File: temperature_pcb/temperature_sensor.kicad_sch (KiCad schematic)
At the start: 15 parts, among them J1 Screw_Terminal_01x02, M1 MAX31865-adafruit-module, M10 MAX31865-adafruit-module, M11 MAX31865-adafruit-module, M12 MAX31865-adafruit-module, M13 MAX31865-adafruit-module, M2 MAX31865-adafruit-module, M3 MAX31865-adafruit-module, M4 MAX31865-adafruit-module, M5 MAX31865-adafruit-module, M6 MAX31865-adafruit-module, M7 MAX31865-adafruit-module, M8 MAX31865-adafruit-module, M9 MAX31865-adafruit-module

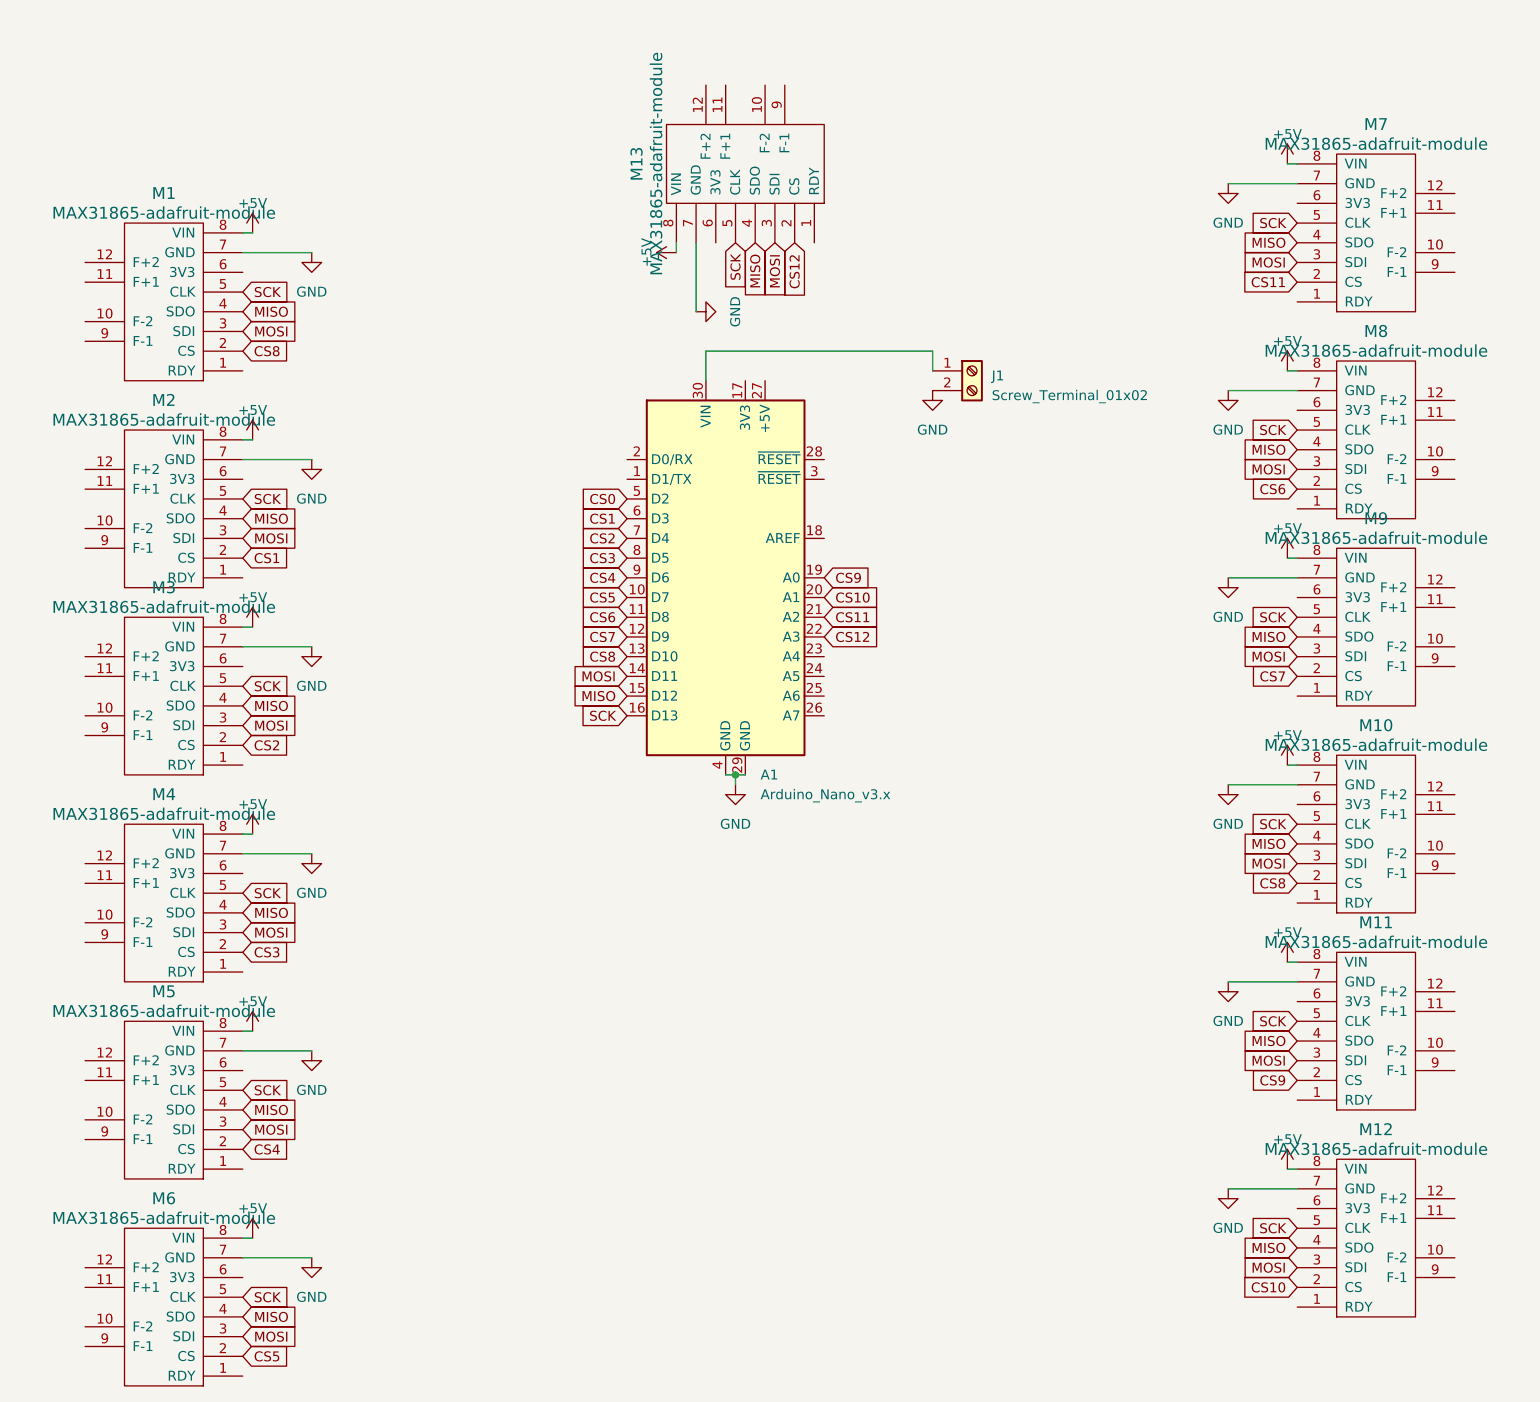
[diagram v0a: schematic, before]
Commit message: first version of the pcb for the temperature sensors
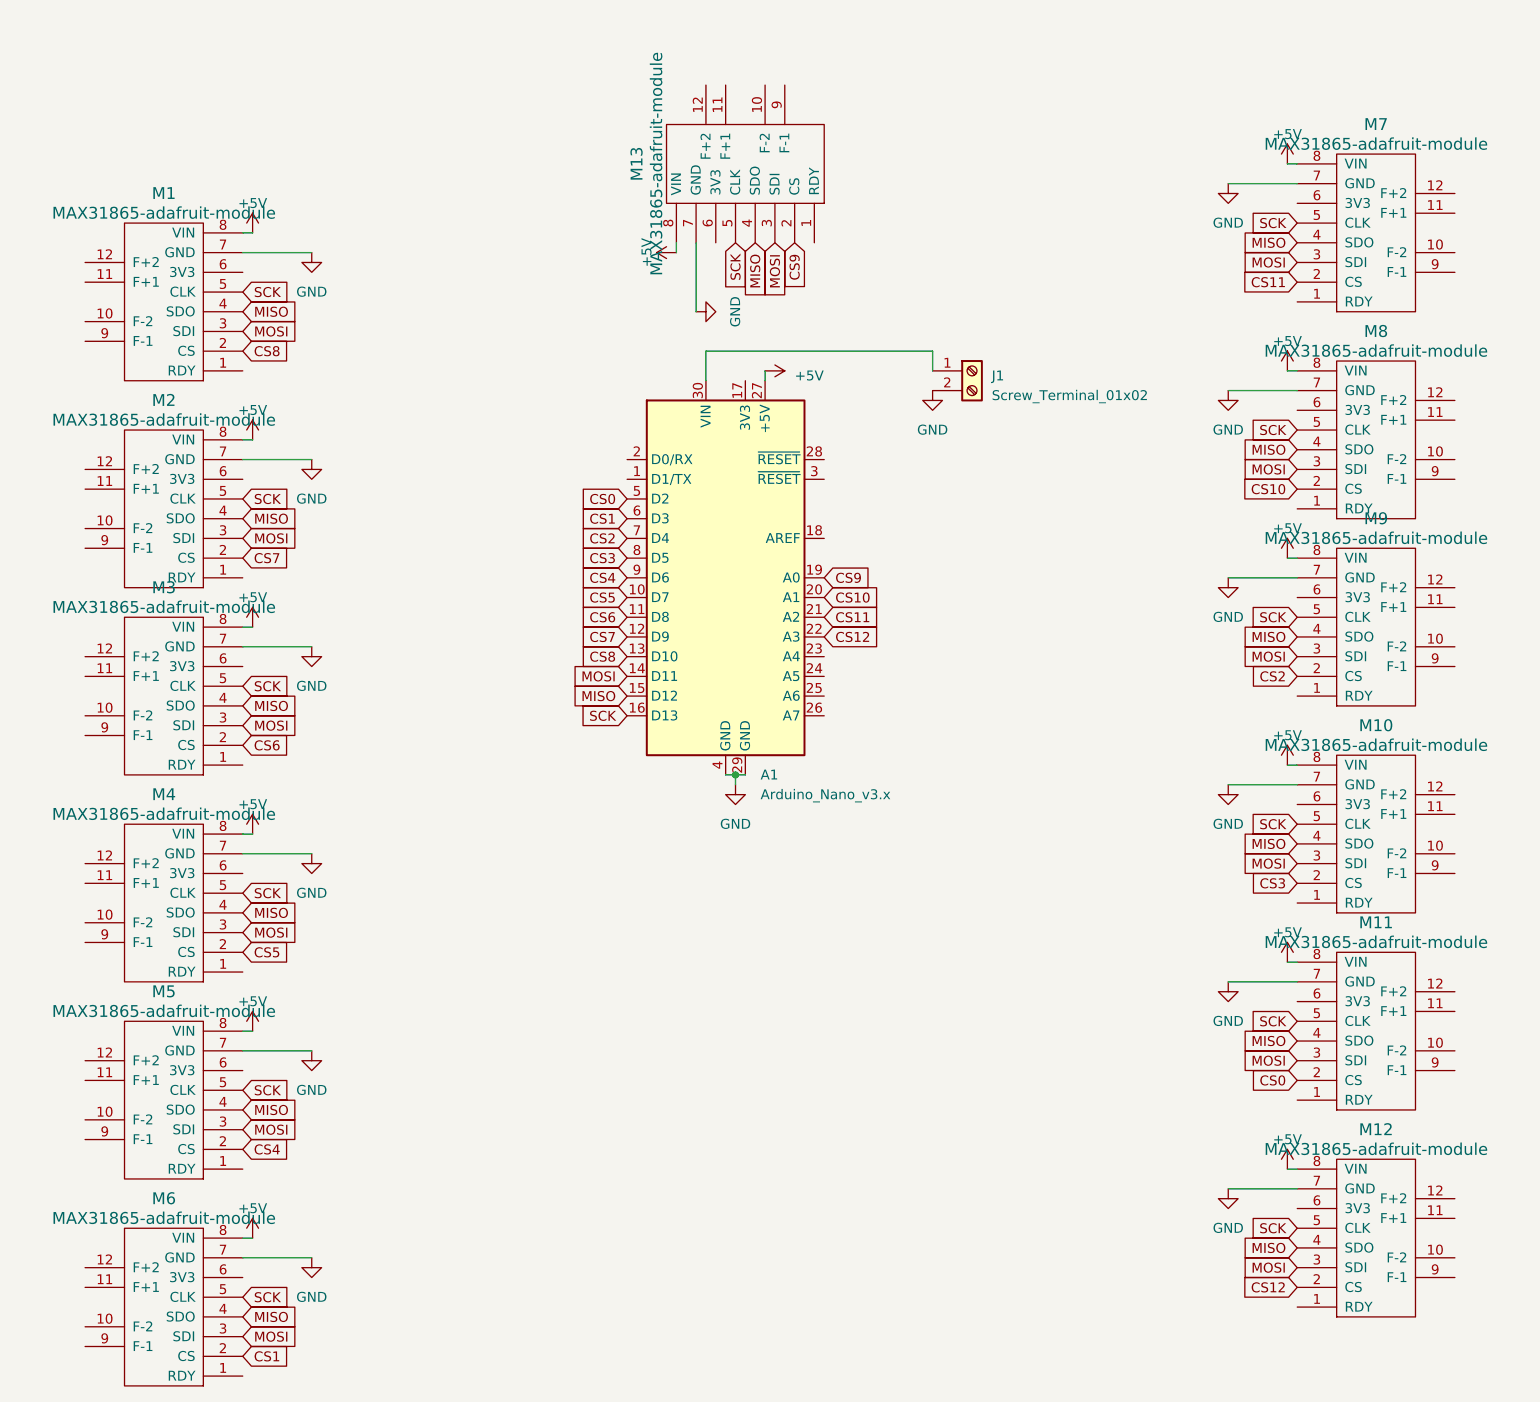
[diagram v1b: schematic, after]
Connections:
- net +5V: now also A1.27 (+5V)
- net CS0: now also M11.2 (CS)
- net CS1: now also M6.2 (CS); no longer M2.2 (CS)
- net CS10: now also M8.2 (CS); no longer M12.2 (CS)
- net CS12: now also M12.2 (CS); no longer M13.2 (CS)
- net CS2: now also M9.2 (CS); no longer M3.2 (CS)
- net CS3: now also M10.2 (CS); no longer M4.2 (CS)
- net CS5: now also M4.2 (CS); no longer M6.2 (CS)
- net CS6: now also M3.2 (CS); no longer M8.2 (CS)
- net CS7: now also M2.2 (CS); no longer M9.2 (CS)
- net CS8: no longer M10.2 (CS)
- net CS9: now also M13.2 (CS); no longer M11.2 (CS)
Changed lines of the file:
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@@
+    (stroke (width 0) (type default))
+  )
+  (wire (pts (xy 140.97 55.88) (xy 140.97 57.15))
     (stroke (width 0) (type default))
   )
@@
     )
   )
-  (global_label "CS2" (shape input) (at 73.66 104.14 0) (fields_autoplaced)
+  (global_label "CS6" (shape input) (at 73.66 104.14 0) (fields_autoplaced)
     (effects (font (size 1.27 1.27)) (justify left))
     (property "Intersheetrefs" "${INTERSHEET_REFS}" (at 80.2548 104.14 0)
@@
     )
   )
-  (global_label "CS12" (shape input) (at 144.78 39.37 270) (fields_autoplaced)
-    (effects (font (size 1.27 1.27)) (justify right))
-    (property "Intersheetrefs" "${INTERSHEET_REFS}" (at 144.78 47.1743 90)
+  (global_label "CS9" (shape input) (at 144.78 39.37 270) (fields_autoplaced)
+    (effects (font (size 1.27 1.27)) (justify right))
+    (property "Intersheetrefs" "${INTERSHEET_REFS}" (at 144.78 45.9648 90)
       (effects (font (size 1.27 1.27)) (justify right) hide)
     )
@@
     )
   )
-  (global_label "CS7" (shape input) (at 209.55 95.25 180) (fields_autoplaced)
+  (global_label "CS2" (shape input) (at 209.55 95.25 180) (fields_autoplaced)
     (effects (font (size 1.27 1.27)) (justify right))
     (property "Intersheetrefs" "${INTERSHEET_REFS}" (at 202.9552 95.25 0)
@@
     )
   )
-  (global_label "CS10" (shape input) (at 209.55 173.99 180) (fields_autoplaced)
+  (global_label "CS12" (shape input) (at 209.55 173.99 180) (fields_autoplaced)
     (effects (font (size 1.27 1.27)) (justify right))
     (property "Intersheetrefs" "${INTERSHEET_REFS}" (at 201.7457 173.99 0)
@@
     )
   )
-  (global_label "CS9" (shape input) (at 209.55 147.32 180) (fields_autoplaced)
+  (global_label "CS0" (shape input) (at 209.55 147.32 180) (fields_autoplaced)
     (effects (font (size 1.27 1.27)) (justify right))
     (property "Intersheetrefs" "${INTERSHEET_REFS}" (at 202.9552 147.32 0)
@@
     )
   )
-  (global_label "CS1" (shape input) (at 73.66 80.01 0) (fields_autoplaced)
+  (global_label "CS7" (shape input) (at 73.66 80.01 0) (fields_autoplaced)
     (effects (font (size 1.27 1.27)) (justify left))
     (property "Intersheetrefs" "${INTERSHEET_REFS}" (at 80.2548 80.01 0)
@@
     )
   )
-  (global_label "CS5" (shape input) (at 73.66 182.88 0) (fields_autoplaced)
+  (global_label "CS1" (shape input) (at 73.66 182.88 0) (fields_autoplaced)
     (effects (font (size 1.27 1.27)) (justify left))
     (property "Intersheetrefs" "${INTERSHEET_REFS}" (at 80.2548 182.88 0)
@@
     )
   )
-  (global_label "CS8" (shape input) (at 209.55 121.92 180) (fields_autoplaced)
+  (global_label "CS3" (shape input) (at 209.55 121.92 180) (fields_autoplaced)
     (effects (font (size 1.27 1.27)) (justify right))
     (property "Intersheetrefs" "${INTERSHEET_REFS}" (at 202.9552 121.92 0)
@@
     )
   )
-  (global_label "CS6" (shape input) (at 209.55 71.12 180) (fields_autoplaced)
-    (effects (font (size 1.27 1.27)) (justify right))
-    (property "Intersheetrefs" "${INTERSHEET_REFS}" (at 202.9552 71.12 0)
+  (global_label "CS10" (shape input) (at 209.55 71.12 180) (fields_autoplaced)
+    (effects (font (size 1.27 1.27)) (justify right))
+    (property "Intersheetrefs" "${INTERSHEET_REFS}" (at 201.7457 71.12 0)
       (effects (font (size 1.27 1.27)) (justify right) hide)
     )
@@
     )
   )
-  (global_label "CS3" (shape input) (at 73.66 130.81 0) (fields_autoplaced)
+  (global_label "CS5" (shape input) (at 73.66 130.81 0) (fields_autoplaced)
     (effects (font (size 1.27 1.27)) (justify left))
     (property "Intersheetrefs" "${INTERSHEET_REFS}" (at 80.2548 130.81 0)
@@
         )
       )
+    )
+  )
+  (symbol (lib_id "power:+5V") (at 140.97 55.88 270) (mirror x) (unit 1)
+    (in_bom yes) (on_board yes) (dnp no) (fields_autoplaced)
+    (property "Reference" "#PWR029" (at 137.16 55.88 0)
+      (effects (font (size 1.27 1.27)) hide)
+    )
+    (property "Value" "+5V" (at 144.78 56.515 90)
+      (effects (font (size 1.27 1.27)) (justify left))
+    )
+    (property "Footprint" "" (at 140.97 55.88 0)
+      (effects (font (size 1.27 1.27)) hide)
+    )
+    (property "Datasheet" "" (at 140.97 55.88 0)
+      (effects (font (size 1.27 1.27)) hide)
+    )
+    (pin "1")
+    (instances
+      (project "temperature_sensor"
+        (path "/3b3a792b-3989-474d-9099-a36c74963482"
+          (reference "#PWR029") (unit 1)
+        )
+      )
